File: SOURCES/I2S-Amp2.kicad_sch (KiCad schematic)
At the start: 34 parts, among them P14 CONN_01X02, P15 CONN_01X02, P21 TST, U8 SN74LVC14ADG4, U9 TAS5760MDCAR

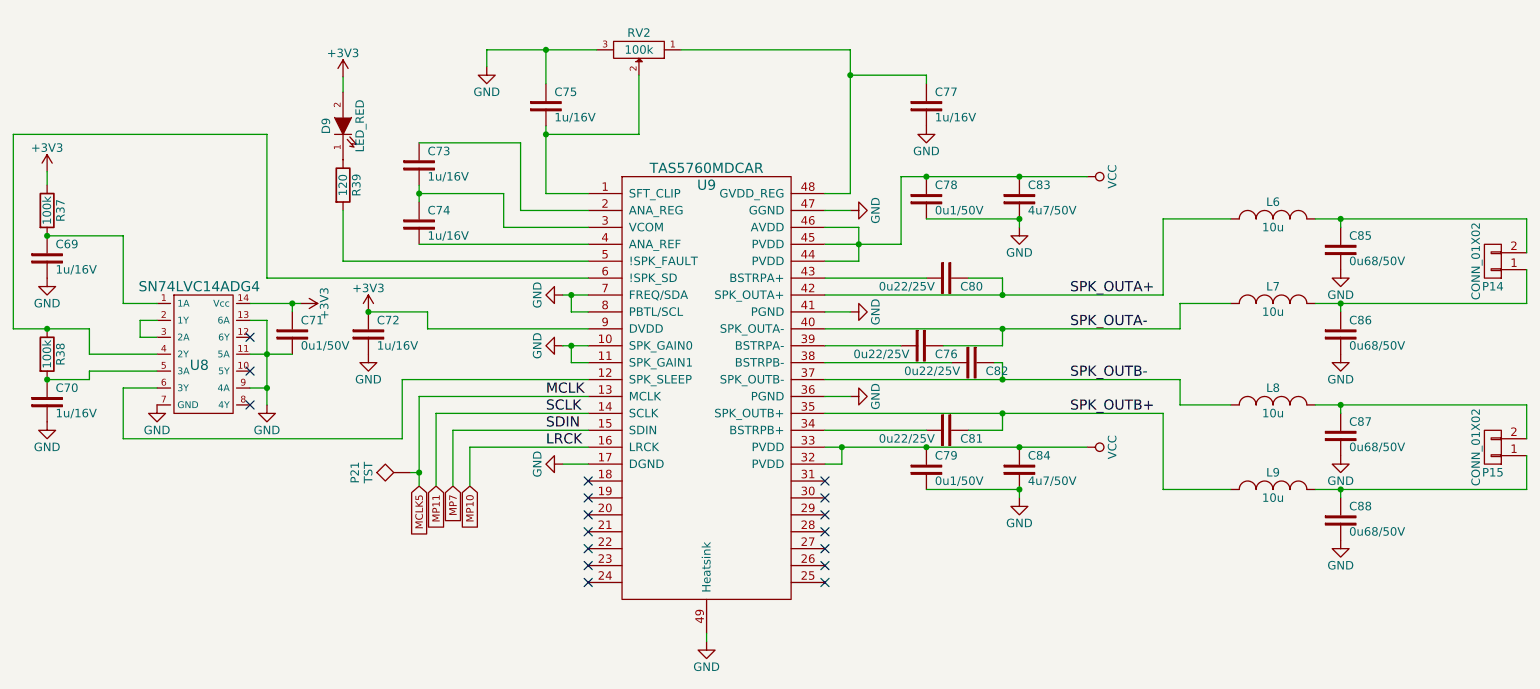
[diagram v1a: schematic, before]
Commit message: Removed redundant 7414 and pot, rerouted a bit.
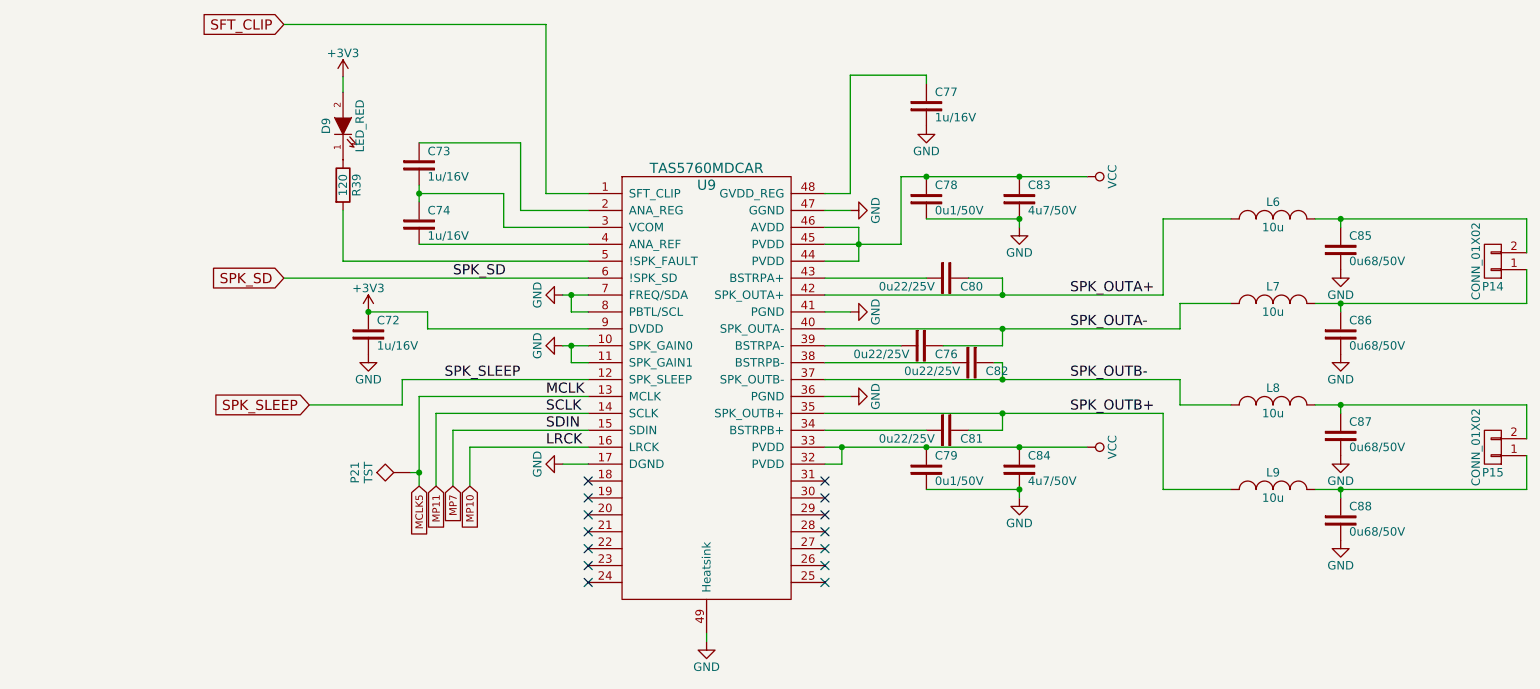
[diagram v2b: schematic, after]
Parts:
- removed C69, C70, C75: 1u/16V, fdsp_capacitor:C_1206_HandSoldering, symbol MyLibrary:Capacitor
- removed C71: 0u1/50V, fdsp_capacitor:C_1206_HandSoldering, symbol MyLibrary:Capacitor
- removed R37, R38: 100k, fdsp_resistor:R_1206_HandSoldering, symbol smd_aio-rescue:R
- removed RV2: 100k, AMPx2 _footprints:M64Z104KB40, symbol smd_aio-rescue:POT
- removed U8: SN74LVC14ADG4, Housings_SOIC:SOIC-14_3.9x8.7mm_Pitch1.27mm, symbol MyLibrary:SN74LVC14ADG4
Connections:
- net SPK_SD: now reaches U9.6 (!SPK_SD)
- net SPK_SLEEP: now reaches U9.12 (SPK_SLEEP)
- net SFT_CLIP: now reaches U9.1 (SFT_CLIP)
- no-connect marks 17 -> 14

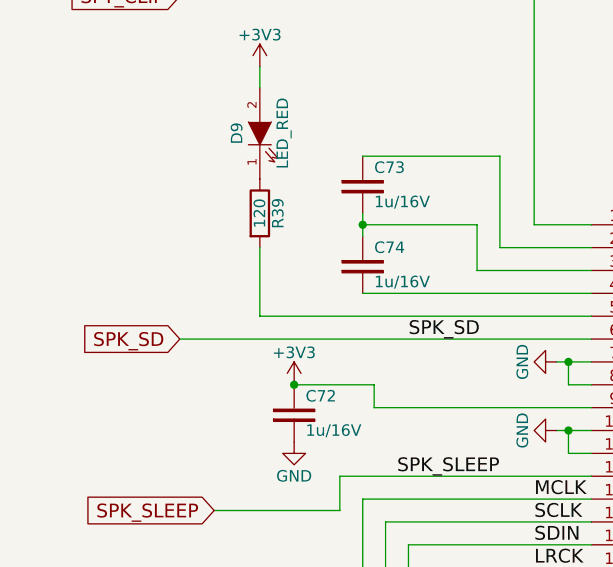
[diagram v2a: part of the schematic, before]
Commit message: Removed ArduinoPort, Changed Power Supply. Rerouting and stuff.
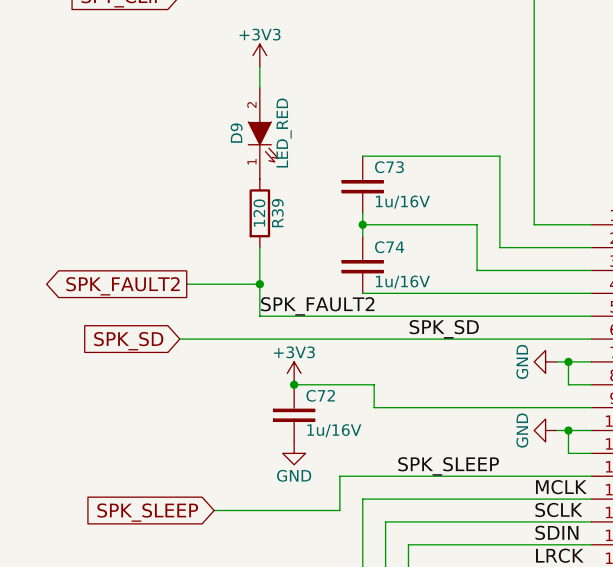
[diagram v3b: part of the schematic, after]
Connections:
- net SPK_FAULT2: now reaches R39.2, U9.5 (!SPK_FAULT)
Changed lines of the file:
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@@
   (junction (at 179.07 45.72) (diameter 0) (color 0 0 0 0)
+  )
+  (junction (at 91.44 54.864) (diameter 0) (color 0 0 0 0)
   )
   (junction (at 102.87 48.26) (diameter 0) (color 0 0 0 0)
@@
     (stroke (width 0) (type default))
   )
+  (wire (pts (xy 83.312 54.864) (xy 91.44 54.864))
+    (stroke (width 0) (type default))
+  )
   (wire (pts (xy 125.73 66.04) (xy 125.73 63.5))
     (stroke (width 0) (type default))
@@
     (stroke (width 0) (type default))
   )
-  (wire (pts (xy 91.44 58.42) (xy 91.44 50.8))
+  (wire (pts (xy 91.44 58.42) (xy 91.44 54.864))
     (stroke (width 0) (type default))
   )
@@
     (stroke (width 0) (type default))
   )
+  (wire (pts (xy 91.44 54.864) (xy 91.44 50.8))
+    (stroke (width 0) (type default))
+  )
   (wire (pts (xy 102.87 40.64) (xy 118.11 40.64))
     (stroke (width 0) (type default))
@@
   (wire (pts (xy 128.27 86.36) (xy 110.49 86.36))
     (stroke (width 0) (type default))
+  )
+  (label "SPK_FAULT2" (at 91.44 58.42 0) (fields_autoplaced)
+    (effects (font (size 1.524 1.524)) (justify left bottom))
   )
   (label "SPK_OUTB+" (at 200.66 81.28 0) (fields_autoplaced)
@@
     )
   )
+  (global_label "SPK_FAULT2" (shape output) (at 83.312 54.864 180) (fields_autoplaced)
+    (effects (font (size 1.524 1.524)) (justify right))
+    (property "Intersheetrefs" "${INTERSHEET_REFS}" (at 66.7993 54.864 0)
+      (effects (font (size 1.27 1.27)) (justify right) hide)
+    )
+  )

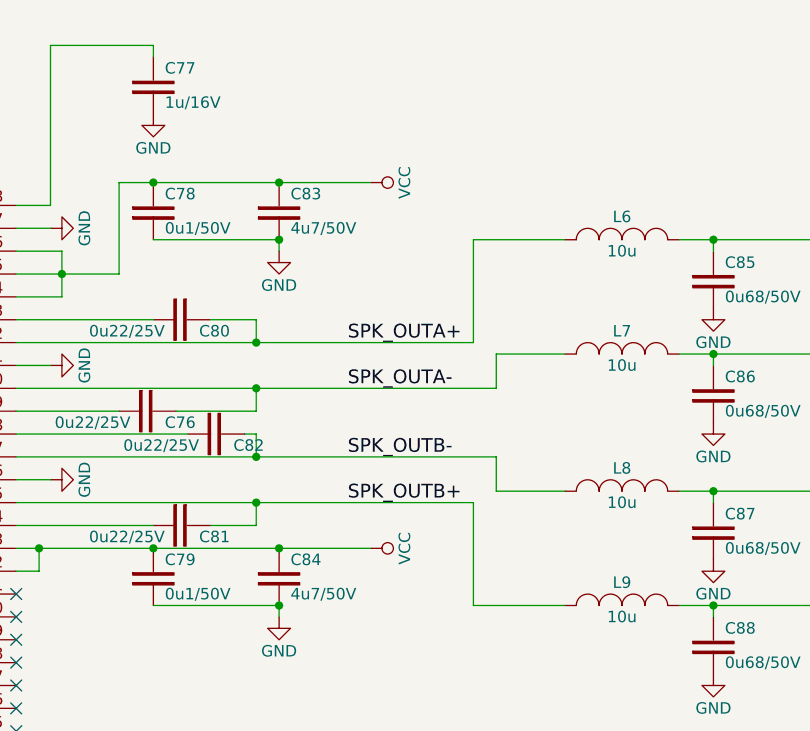
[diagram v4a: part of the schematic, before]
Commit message: Fixed Vin/Vcc issue.
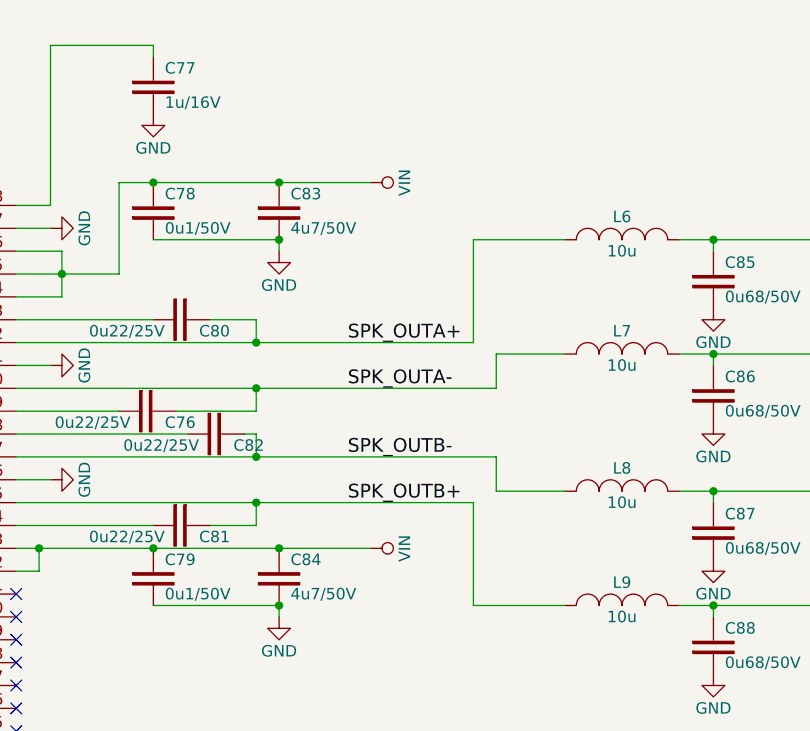
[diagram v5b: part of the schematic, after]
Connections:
- net VCC renamed VIN
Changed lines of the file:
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@@
 			)
 		)
-		(property "Value" "VCC"
+		(property "Value" "VIN"
 			(at 207.01 45.72 0)
 			(effects
@@
 			)
 		)
-		(property "Value" "VCC"
+		(property "Value" "VIN"
 			(at 207.01 86.36 0)
 			(effects

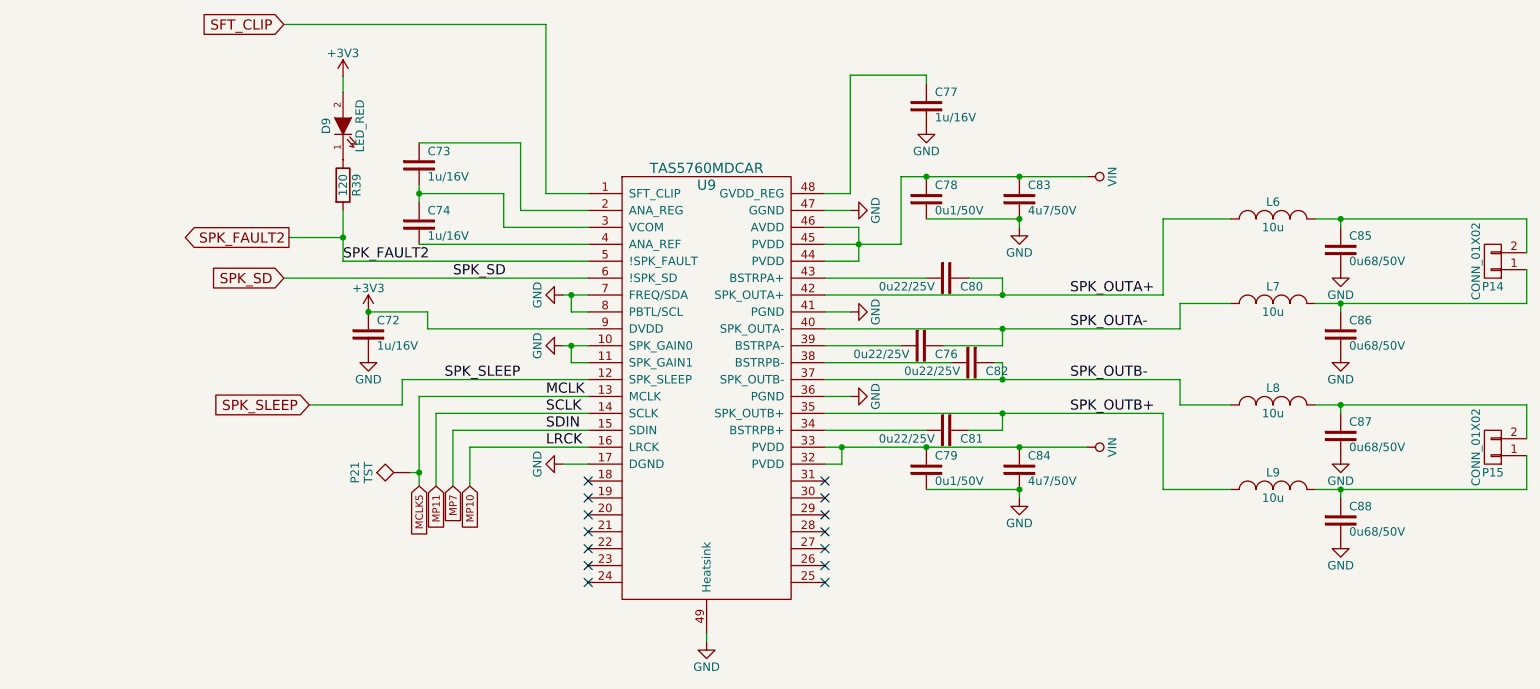
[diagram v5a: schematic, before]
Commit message: Improved power traces.
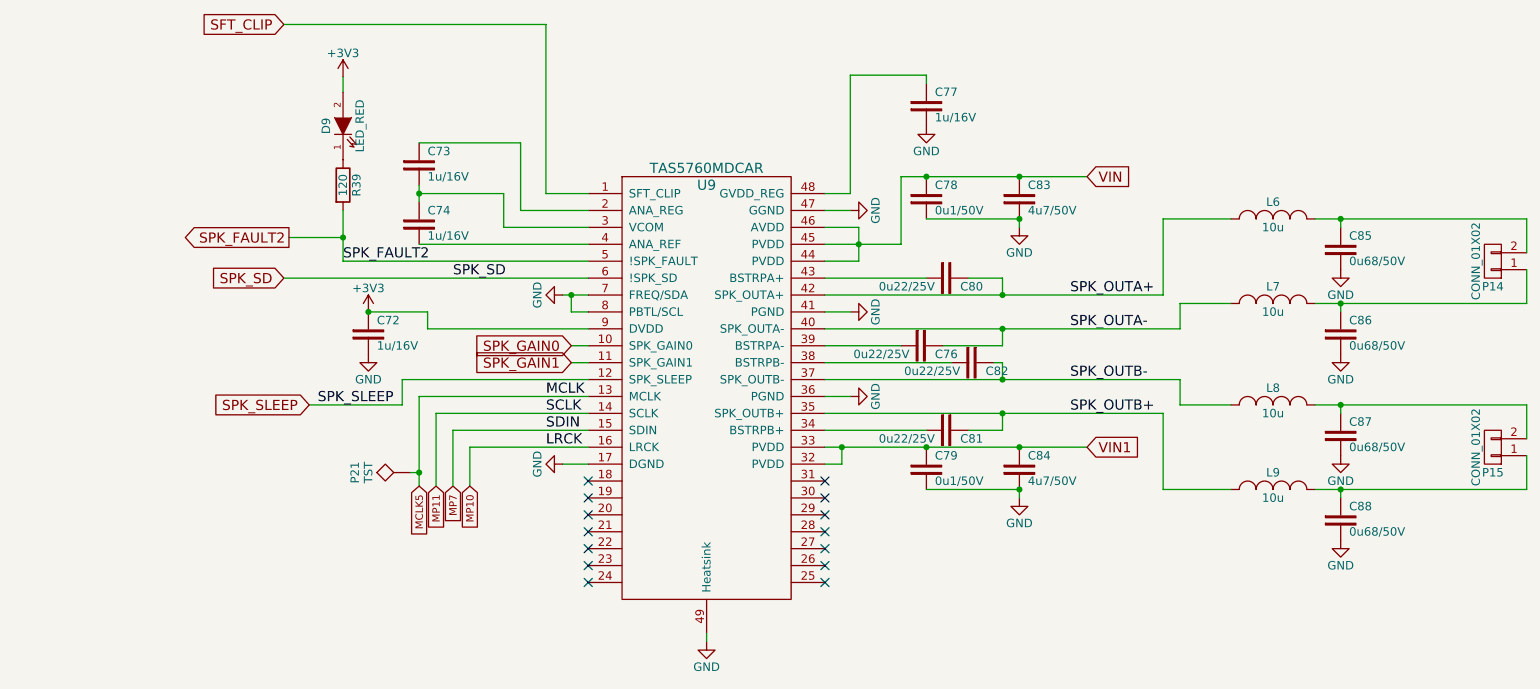
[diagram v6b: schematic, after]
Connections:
- net GND: no longer U9.10 (SPK_GAIN0), U9.11 (SPK_GAIN1)
- net VIN: no longer C79.1, C84.1, U9.32 (PVDD), U9.33 (PVDD)
- new net SPK_GAIN0: U9.10 (SPK_GAIN0)
- new net SPK_GAIN1: U9.11 (SPK_GAIN1)
- new net VIN1: C79.1, C84.1, U9.32 (PVDD), U9.33 (PVDD)
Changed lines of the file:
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@@
 	)
 	(junction
-		(at 125.73 71.12)
-		(diameter 0)
-		(color 0 0 0 0)
-	)
-	(junction
 		(at 190.5 76.2)
 		(diameter 0)
@@
 	(wire
 		(pts
+			(xy 100.33 80.01) (xy 100.33 76.2)
+		)
+		(stroke
+			(width 0)
+			(type default)
+		)
+	)
+	(wire
+		(pts
 			(xy 190.5 73.66) (xy 190.5 76.2)
 		)
@@
 	(wire
 		(pts
-			(xy 125.73 71.12) (xy 128.27 71.12)
-		)
-		(stroke
-			(width 0)
-			(type default)
-		)
-	)
-	(wire
-		(pts
-			(xy 100.33 80.01) (xy 86.36 80.01)
+			(xy 86.36 80.01) (xy 100.33 80.01)
 		)
 		(stroke
@@
 	(wire
 		(pts
-			(xy 125.73 73.66) (xy 125.73 71.12)
-		)
-		(stroke
-			(width 0)
-			(type default)
-		)
-	)
-	(wire
-		(pts
 			(xy 237.49 80.01) (xy 241.3 80.01)
 		)
@@
 	(wire
 		(pts
-			(xy 124.46 71.12) (xy 125.73 71.12)
+			(xy 124.46 63.5) (xy 125.73 63.5)
 		)
 		(stroke
@@
 	(wire
 		(pts
-			(xy 124.46 63.5) (xy 125.73 63.5)
+			(xy 163.83 86.36) (xy 166.37 86.36)
 		)
 		(stroke
@@
 	(wire
 		(pts
-			(xy 100.33 80.01) (xy 100.33 76.2)
+			(xy 125.73 73.66) (xy 128.27 73.66)
 		)
 		(stroke
@@
 	(wire
 		(pts
-			(xy 163.83 86.36) (xy 166.37 86.36)
+			(xy 125.73 71.12) (xy 128.27 71.12)
 		)
 		(stroke
@@
 	(wire
 		(pts
-			(xy 128.27 73.66) (xy 125.73 73.66)
-		)
-		(stroke
-			(width 0)
-			(type default)
-		)
-	)
-	(wire
-		(pts
 			(xy 190.5 63.5) (xy 214.63 63.5)
 		)
@@
 	)
 	(label "SPK_SLEEP"
-		(at 106.68 76.2 0)
+		(at 87.63 80.01 0)
 		(fields_autoplaced yes)
 		(effects
@@
 		)
 	)
+	(global_label "SPK_GAIN0"
+		(shape input)
+		(at 125.73 71.12 180)
+		(fields_autoplaced yes)
+		(effects
+			(font
+				(size 1.524 1.524)
+			)
+			(justify right)
+		)
+		(property "Intersheetrefs" "${INTERSHEET_REFS}"
+			(at 110.6687 71.12 0)
+			(effects
+				(font
+					(size 1.27 1.27)
+				)
+				(justify right)
+				(hide yes)
+			)
+		)
+	)
 	(global_label "MCLK5"
 		(shape input)
@@
 		)
 	)
+	(global_label "SPK_GAIN1"
+		(shape input)
+		(at 125.73 73.66 180)
+		(fields_autoplaced yes)
+		(effects
+			(font
+				(size 1.524 1.524)
+			)
+			(justify right)
+		)
+		(property "Intersheetrefs" "${INTERSHEET_REFS}"
+			(at 110.6687 73.66 0)
+			(effects
+				(font
+					(size 1.27 1.27)
+				)
+				(justify right)
+				(hide yes)
+			)
+		)
+	)
+	(global_label "VIN1"
+		(shape input)
+		(at 203.2 86.36 0)
+		(fields_autoplaced yes)
+		(effects
+			(font
+				(size 1.524 1.524)
+			)
+			(justify left)
+		)
+		(property "Intersheetrefs" "${INTERSHEET_REFS}"
+			(at 211.0768 86.36 0)
+			(effects
+				(font
+					(size 1.27 1.27)
+				)
+				(justify left)
+				(hide yes)
+			)
+		)
+	)
 	(global_label "SFT_CLIP"
 		(shape input)
@@
 		)
 	)
+	(global_label "VIN"
+		(shape input)
+		(at 203.2 45.72 0)
+		(fields_autoplaced yes)
+		(effects
+			(font
+				(size 1.524 1.524)
+			)
+			(justify left)
+		)
+		(property "Intersheetrefs" "${INTERSHEET_REFS}"
+			(at 209.6254 45.72 0)
+			(effects
+				(font
+					(size 1.27 1.27)
+				)
+				(justify left)
+				(hide yes)
+			)
+		)
+	)
 	(symbol
 		(lib_id "MyLibrary:Capacitor")
@@
 	)
 	(symbol
-		(lib_id "smd_aio-rescue:VCC")
-		(at 203.2 45.72 270)
-		(unit 1)
-		(exclude_from_sim no)
-		(in_bom yes)
-		(on_board yes)
-		(dnp no)
-		(property "Reference" "#PWR0134"
-			(at 199.39 45.72 0)
-			(effects
-				(font
-					(size 1.27 1.27)
-				)
-				(hide yes)
-			)
-		)
-		(property "Value" "VIN"
-			(at 207.01 45.72 0)
-			(effects
-				(font
-					(size 1.27 1.27)
-				)
-			)
-		)
-		(property "Footprint" ""
-			(at 203.2 45.72 0)
-			(effects
-				(font
-					(size 1.27 1.27)
-				)
-			)
-		)
-		(property "Datasheet" ""
-			(at 203.2 45.72 0)
-			(effects
-				(font
-					(size 1.27 1.27)
-				)
-			)
-		)
-		(property "Description" ""
-			(at 203.2 45.72 0)
-			(effects
-				(font
-					(size 1.27 1.27)
-				)
-				(hide yes)
-			)
-		)
-		(pin "1"
-		)
-		(instances
-			(project "smd_aio"
-				(path "/4c49a07c-9ad4-4758-901a-e68e360dc17d/00000000-0000-0000-0000-00005b04b659"
-					(reference "#PWR0134")
-					(unit 1)
-				)
-			)
-		)
-	)
-	(symbol
 		(lib_id "smd_aio-rescue:CONN_01X02")
 		(at 264.16 58.42 180)
@@
 	(symbol
 		(lib_id "smd_aio-rescue:GND")
-		(at 124.46 71.12 270)
-		(unit 1)
-		(exclude_from_sim no)
-		(in_bom yes)
-		(on_board yes)
-		(dnp no)
-		(property "Reference" "#PWR0128"
-			(at 118.11 71.12 0)
-			(effects
-				(font
-					(size 1.27 1.27)
-				)
-				(hide yes)
-			)
-		)
-		(property "Value" "GND"
-			(at 120.65 71.12 0)
-			(effects
-				(font
-					(size 1.27 1.27)
-				)
-			)
-		)
-		(property "Footprint" ""
-			(at 124.46 71.12 0)
-			(effects
-				(font
-					(size 1.27 1.27)
-				)
-			)
-		)
-		(property "Datasheet" ""
-			(at 124.46 71.12 0)
-			(effects
-				(font
-					(size 1.27 1.27)
-				)
-			)
-		)
-		(property "Description" ""
-			(at 124.46 71.12 0)
-			(effects
-				(font
-					(size 1.27 1.27)
-				)
-				(hide yes)
-			)
-		)
-		(pin "1"
-		)
-		(instances
-			(project "smd_aio"
-				(path "/4c49a07c-9ad4-4758-901a-e68e360dc17d/00000000-0000-0000-0000-00005b04b659"
-					(reference "#PWR0128")
-					(unit 1)
-				)
-			)
-		)
-	)
-	(symbol
-		(lib_id "smd_aio-rescue:GND")
 		(at 124.46 63.5 270)
 		(unit 1)
@@
 					(unit 1)
 				)
-			)
-		)
-	)
-	(symbol
-		(lib_id "smd_aio-rescue:VCC")
-		(at 203.2 86.36 270)
-		(unit 1)
-		(exclude_from_sim no)
-		(in_bom yes)
-		(on_board yes)
-		(dnp no)
-		(property "Reference" "#PWR0130"
-			(at 199.39 86.36 0)
-			(effects
-				(font
-					(size 1.27 1.27)
-				)
-				(hide yes)
-			)
-		)
-		(property "Value" "VIN"
-			(at 207.01 86.36 0)
-			(effects
-				(font
-					(size 1.27 1.27)
-				)
-			)
-		)
-		(property "Footprint" ""
-			(at 203.2 86.36 0)
-			(effects
-				(font
-					(size 1.27 1.27)
-				)
-			)
-		)
-		(property "Datasheet" ""
-			(at 203.2 86.36 0)
-			(effects
-				(font
-					(size 1.27 1.27)
-				)
-			)
-		)
-		(property "Description" ""
-			(at 203.2 86.36 0)
-			(effects
-				(font
-					(size 1.27 1.27)
-				)
-				(hide yes)
-			)
-		)
-		(pin "1"
-		)
-		(instances
-			(project "smd_aio"
-				(path "/4c49a07c-9ad4-4758-901a-e68e360dc17d/00000000-0000-0000-0000-00005b04b659"
-					(reference "#PWR0130")
-					(unit 1)
-				)
